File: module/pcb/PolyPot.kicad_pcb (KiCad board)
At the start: 2 copper layers, 50 x 50 mm, 34 parts, among them J1 V_BAT_1S, J2 PROG/DEBUG, J3 ANALOG_CONN, J4 TOF_DIST_SENS, J5 M3, J6 M3, J7 M3, J8 M3, M1 DC_WATER_PUMP, Q1 Q_NMOS_DGS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

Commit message: Update pin assignment, add user button, add luminosity conn
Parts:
- added J9: LUMINOSITY_CONN, Socket_Strips:Socket_Strip_Straight_1x03_Pitch2.00mm, F.Cu at (63.5, 103.0)
- added R7, R9: 10k, Resistors_SMD:R_0603_HandSoldering, F.Cu at (55.0, 90.1)
- added R8: 470, Resistors_SMD:R_0603_HandSoldering, F.Cu at (55.0, 90.1)
- added SW3: USR_BTN, Socket_Strips:Socket_Strip_Straight_1x02_Pitch2.00mm, F.Cu at (72.3, 92.0)
- added TP5: TEST, Socket_Strips:Socket_Strip_Straight_1x01_Pitch1.27mm, F.Cu at (55.0, 90.1)
- J3: value ANALOG_CONN -> HUMIDITY_CONN
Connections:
- D1 pad 2: (no net) -> /LED_STATUS
- J1 pad 1: (no net) -> /V_BAT_SENSE
- J3 pad 2: (no net) -> /SENS_HUMIDITY
- Q1 pad 2: (no net) -> /PUMP_PWM
- R3 pad 1: +3V3 -> (no net)
- U2 pad 1: (no net) -> GND
- U2 pad 12: (no net) -> /PUMP_PWM
- U2 pad 13: (no net) -> /LED_STATUS
- U2 pad 14: (no net) -> /SENSORS_ENn
- U2 pad 24: (no net) -> Net-(R7-Pad2)
- U2 pad 30: (no net) -> /I2C_SDA
- U2 pad 31: (no net) -> /I2C_SCL
- U2 pad 35: /UART_TX -> Net-(R8-Pad1)
- U2 pad 39: (no net) -> GND
- U2 pad 7: (no net) -> /V_BAT_SENSE
- U2 pad 8: (no net) -> /SENS_HUMIDITY
- U2 pad 9: (no net) -> /SENS_LUMINOSITY

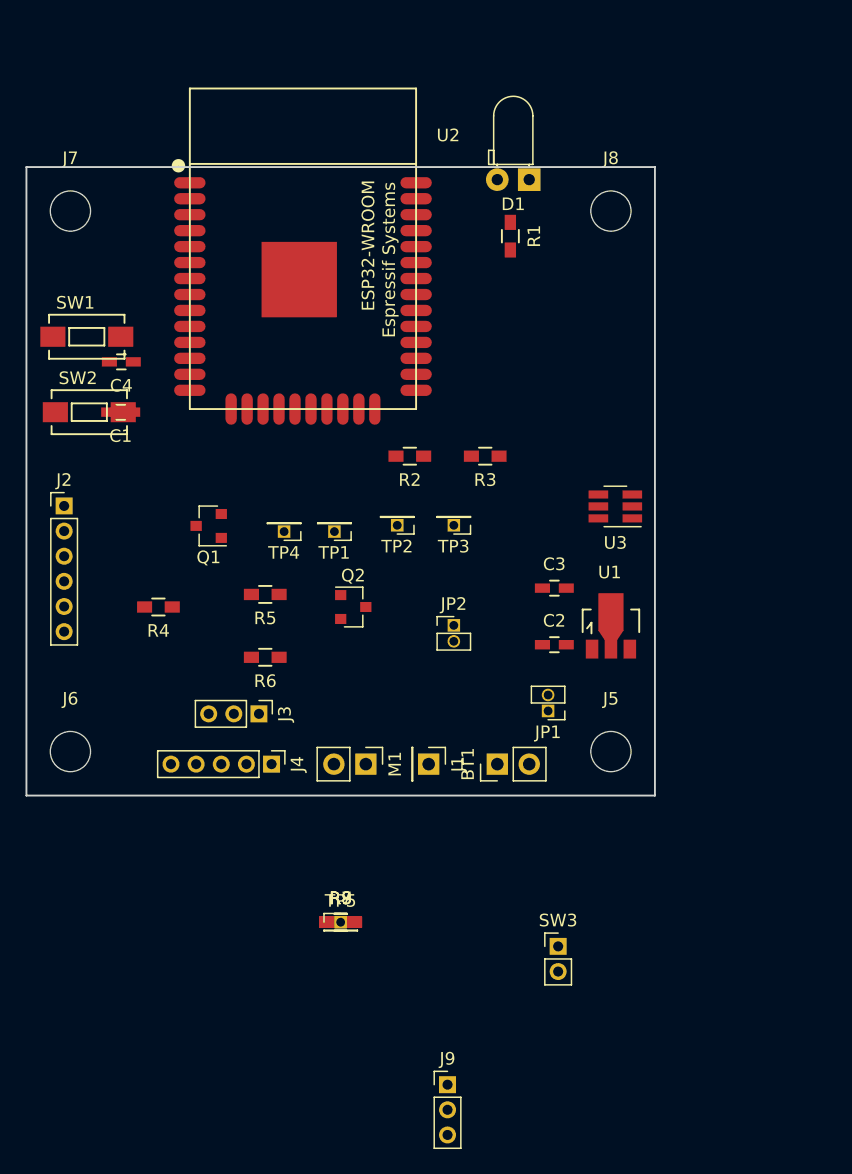
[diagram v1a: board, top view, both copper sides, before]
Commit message: PCB: update voltage regulator
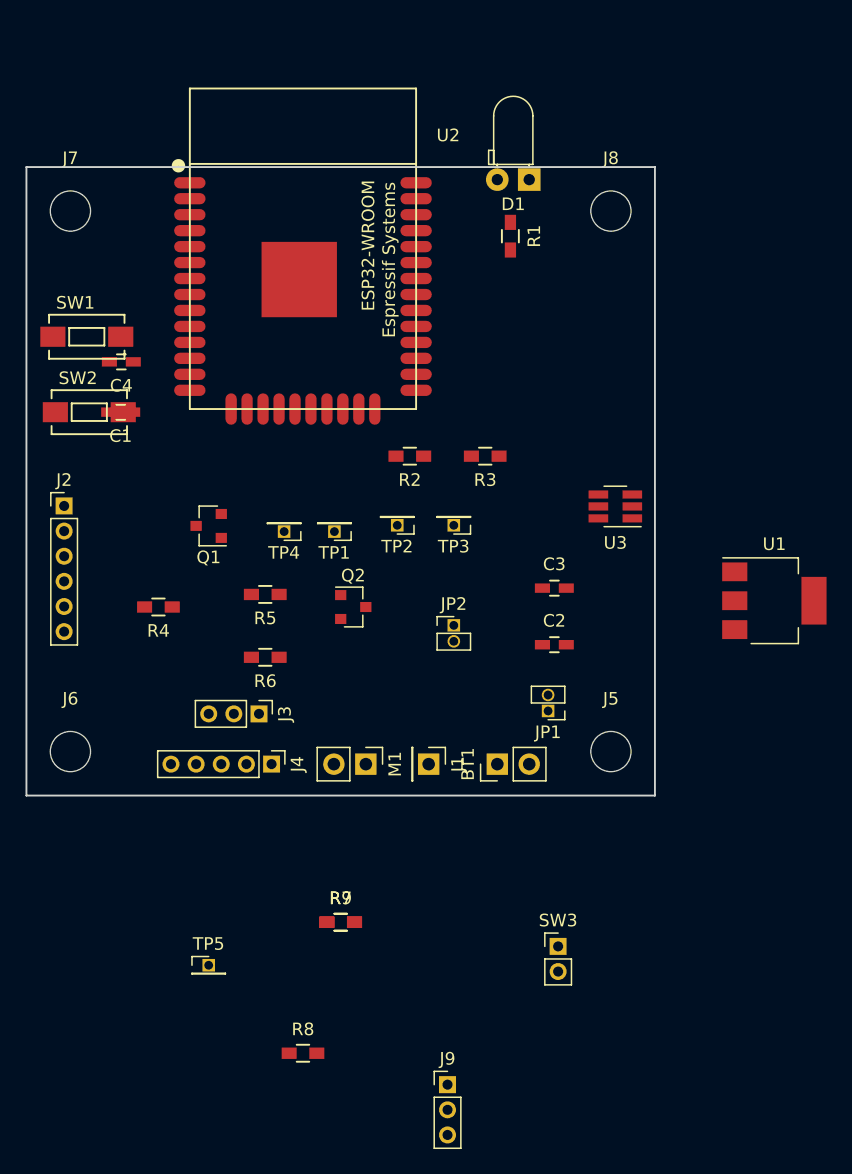
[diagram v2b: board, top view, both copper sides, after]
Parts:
- U1: value MCP1703A-3002_SOT89 -> AP7365-XXEG_SOT223; footprint TO_SOT_Packages_SMD:SOT89-3_Housing -> TO_SOT_Packages_SMD:SOT-223
- moved U1 13.2 mm to (89.5, 64.5)
- moved TP5 11.0 mm to (44.5, 93.5)
- moved R8 10.8 mm to (52.0, 100.5)
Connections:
- U1 pad 1: GND -> +3V3
- U1 pad 2: Net-(C2-Pad1) -> GND
- U1 pad 3: +3V3 -> Net-(C2-Pad1)
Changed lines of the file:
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@@
 (kicad_pcb (version 4) (host pcbnew 4.0.7)
   (general
-    (links 72)
-    (no_connects 72)
+    (links 70)
+    (no_connects 70)
     (area 29.924999 29.924999 80.075001 80.075001)
     (thickness 1.6)
@@
     (pad 1 smd rect (at -2.7 0) (size 2 1.6) (layers F.Cu F.Paste F.Mask)
       (net 2 GND))
-  )
-  (module TO_SOT_Packages_SMD:SOT89-3_Housing (layer F.Cu)
-    (at 76.5 66.5)
-    (descr "SOT89-3, Housing,")
-    (tags "SOT89-3, Housing,")
-    (attr smd)
-    (fp_text reference U1 (at -0.09906 -4.24942) (layer F.SilkS)
-      (effects (font (size 1 1) (thickness 0.15)))
-    )
-    (fp_text value MCP1703A-3002_SOT89 (at -0.20066 4.59994) (layer F.Fab)
-      (effects (font (size 1 1) (thickness 0.15)))
-    )
-    (fp_line (start -1.89992 0.20066) (end -1.651 -0.09906) (layer F.SilkS) (width 0.15))
-    (fp_line (start -1.651 -0.09906) (end -1.5494 -0.24892) (layer F.SilkS) (width 0.15))
-    (fp_line (start -1.5494 -0.24892) (end -1.5494 0.59944) (layer F.SilkS) (width 0.15))
-    (fp_line (start -2.25044 -1.30048) (end -2.25044 0.50038) (layer F.SilkS) (width 0.15))
-    (fp_line (start -2.25044 -1.30048) (end -1.6002 -1.30048) (layer F.SilkS) (width 0.15))
-    (fp_line (start 2.25044 -1.30048) (end 2.25044 0.50038) (layer F.SilkS) (width 0.15))
-    (fp_line (start 2.25044 -1.30048) (end 1.6002 -1.30048) (layer F.SilkS) (width 0.15))
-    (pad 1 smd rect (at -1.50114 1.85166) (size 1.00076 1.50114) (layers F.Cu F.Paste F.Mask)
-      (net 2 GND))
-    (pad 2 smd rect (at 0 1.85166) (size 1.00076 1.50114) (layers F.Cu F.Paste F.Mask)
-      (net 4 "Net-(C2-Pad1)"))
-    (pad 3 smd rect (at 1.50114 1.85166) (size 1.00076 1.50114) (layers F.Cu F.Paste F.Mask)
-      (net 3 +3V3))
-    (pad 2 smd rect (at 0 -1.09982) (size 1.99898 2.99974) (layers F.Cu F.Paste F.Mask)
-      (net 4 "Net-(C2-Pad1)"))
-    (pad 2 smd trapezoid (at 0 0.7493 180) (size 1.50114 0.7493) (rect_delta 0 0.50038 ) (layers F.Cu F.Paste F.Mask)
-      (net 4 "Net-(C2-Pad1)"))
-    (model TO_SOT_Packages_SMD.3dshapes/SOT89-3_Housing.wrl
-      (at (xyz 0 0 0))
-      (scale (xyz 0.3937 0.3937 0.3937))
-      (rotate (xyz 0 0 0))
-    )
   )
   (module PolyPot:ESP32-WROOM (layer F.Cu)
@@
   )
   (module Resistors_SMD:R_0603_HandSoldering (layer F.Cu)
-    (at 55 90.075001)
+    (at 52 100.5)
     (descr "Resistor SMD 0603, hand soldering")
     (tags "resistor 0603")
@@
   )
   (module Socket_Strips:Socket_Strip_Straight_1x01_Pitch1.27mm (layer F.Cu)
-    (at 55 90.075001)
+    (at 44.5 93.5)
     (descr "Through hole straight socket strip, 1x01, 1.27mm pitch, single row")
     (tags "Through hole socket strip THT 1x01 1.27mm single row")
@@
     )
   )
+  (module TO_SOT_Packages_SMD:SOT-223 (layer F.Cu)
+    (at 89.5 64.5)
+    (descr "module CMS SOT223 4 pins")
+    (tags "CMS SOT")
+    (attr smd)
+    (fp_text reference U1 (at 0 -4.5) (layer F.SilkS)
+      (effects (font (size 1 1) (thickness 0.15)))
+    )
+    (fp_text value AP7365-XXEG_SOT223 (at 0 4.5) (layer F.Fab)
+      (effects (font (size 1 1) (thickness 0.15)))
+    )
+    (fp_line (start 1.91 3.41) (end 1.91 2.15) (layer F.SilkS) (width 0.12))
+    (fp_line (start 1.91 -3.41) (end 1.91 -2.15) (layer F.SilkS) (width 0.12))
+    (fp_line (start 4.4 -3.6) (end -4.4 -3.6) (layer F.CrtYd) (width 0.05))
+    (fp_line (start 4.4 3.6) (end 4.4 -3.6) (layer F.CrtYd) (width 0.05))
+    (fp_line (start -4.4 3.6) (end 4.4 3.6) (layer F.CrtYd) (width 0.05))
+    (fp_line (start -4.4 -3.6) (end -4.4 3.6) (layer F.CrtYd) (width 0.05))
+    (fp_line (start -1.85 -3.35) (end -1.85 3.35) (layer F.Fab) (width 0.15))
+    (fp_line (start -1.85 3.41) (end 1.91 3.41) (layer F.SilkS) (width 0.12))
+    (fp_line (start -1.85 -3.35) (end 1.85 -3.35) (layer F.Fab) (width 0.15))
+    (fp_line (start -4.1 -3.41) (end 1.91 -3.41) (layer F.SilkS) (width 0.12))
+    (fp_line (start -1.85 3.35) (end 1.85 3.35) (layer F.Fab) (width 0.15))
+    (fp_line (start 1.85 -3.35) (end 1.85 3.35) (layer F.Fab) (width 0.15))
+    (pad 4 smd rect (at 3.15 0) (size 2 3.8) (layers F.Cu F.Paste F.Mask))
+    (pad 2 smd rect (at -3.15 0) (size 2 1.5) (layers F.Cu F.Paste F.Mask)
+      (net 2 GND))
+    (pad 3 smd rect (at -3.15 2.3) (size 2 1.5) (layers F.Cu F.Paste F.Mask)
+      (net 4 "Net-(C2-Pad1)"))
+    (pad 1 smd rect (at -3.15 -2.3) (size 2 1.5) (layers F.Cu F.Paste F.Mask)
+      (net 3 +3V3))
+    (model TO_SOT_Packages_SMD.3dshapes/SOT-223.wrl
+      (at (xyz 0 0 0))
+      (scale (xyz 0.4 0.4 0.4))
+      (rotate (xyz 0 0 90))
+    )
+  )

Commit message: PCB: 3d model placement
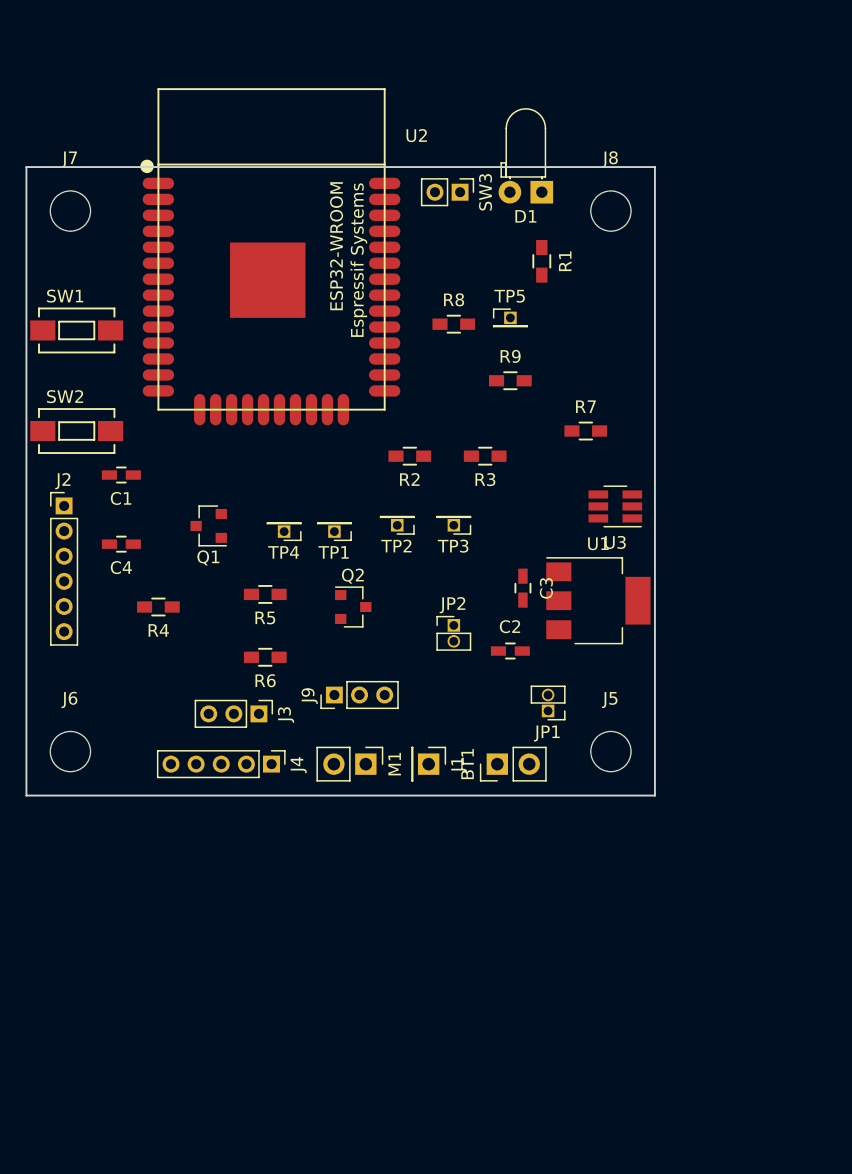
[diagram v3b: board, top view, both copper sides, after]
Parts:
- moved SW3 60.5 mm to (64.5, 32.0), turned to 270 degrees
- moved R8 59.2 mm to (64.0, 42.5)
- moved TP5 56.8 mm to (68.5, 42.0)
- moved R9 45.1 mm to (68.5, 47.0)
- moved R7 43.7 mm to (74.5, 51.0)
- moved J9 32.3 mm to (54.5, 72.0), turned to 90 degrees
- moved C4 14.5 mm to (37.5, 60.0)
- moved U1 14.0 mm to (75.5, 64.5)
- moved C1 5.00 mm to (37.5, 54.5)
- moved C2 3.54 mm to (68.5, 68.5)
- moved R1 3.20 mm to (71.0, 37.5)
- moved U2 2.50 mm to (49.5, 36.5)
- moved C3 2.50 mm to (69.5, 63.5), turned to 270 degrees
- moved SW2 1.80 mm to (34.0, 51.0)
- moved D1 1.41 mm to (71.0, 32.0)
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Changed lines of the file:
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@@
   )
   (module Capacitors_SMD:C_0603_HandSoldering (layer F.Cu)
-    (at 37.5 49.5 180)
+    (at 37.55 54.5 180)
     (descr "Capacitor SMD 0603, hand soldering")
     (tags "capacitor 0603")
@@
   )
   (module Capacitors_SMD:C_0603_HandSoldering (layer F.Cu)
-    (at 72 68)
+    (at 68.5 68.5)
     (descr "Capacitor SMD 0603, hand soldering")
     (tags "capacitor 0603")
@@
   )
   (module Capacitors_SMD:C_0603_HandSoldering (layer F.Cu)
-    (at 72 63.5)
+    (at 69.5 63.5 270)
     (descr "Capacitor SMD 0603, hand soldering")
     (tags "capacitor 0603")
     (attr smd)
-    (fp_text reference C3 (at 0 -1.9) (layer F.SilkS)
-      (effects (font (size 1 1) (thickness 0.15)))
-    )
-    (fp_text value 1uF (at 0 1.9) (layer F.Fab)
+    (fp_text reference C3 (at 0 -1.9 270) (layer F.SilkS)
+      (effects (font (size 1 1) (thickness 0.15)))
+    )
+    (fp_text value 1uF (at 0 1.9 270) (layer F.Fab)
       (effects (font (size 1 1) (thickness 0.15)))
     )
@@
     (fp_line (start -0.35 -0.6) (end 0.35 -0.6) (layer F.SilkS) (width 0.15))
     (fp_line (start 0.35 0.6) (end -0.35 0.6) (layer F.SilkS) (width 0.15))
-    (pad 1 smd rect (at -0.95 0) (size 1.2 0.75) (layers F.Cu F.Paste F.Mask)
+    (pad 1 smd rect (at -0.95 0 270) (size 1.2 0.75) (layers F.Cu F.Paste F.Mask)
       (net 3 +3V3))
-    (pad 2 smd rect (at 0.95 0) (size 1.2 0.75) (layers F.Cu F.Paste F.Mask)
+    (pad 2 smd rect (at 0.95 0 270) (size 1.2 0.75) (layers F.Cu F.Paste F.Mask)
       (net 2 GND))
     (model Capacitors_SMD.3dshapes/C_0603_HandSoldering.wrl
@@
   )
   (module Capacitors_SMD:C_0603_HandSoldering (layer F.Cu)
-    (at 37.55 45.5 180)
+    (at 37.55 60 180)
     (descr "Capacitor SMD 0603, hand soldering")
     (tags "capacitor 0603")
@@
       (at (xyz 0 0 0))
       (scale (xyz 1 1 1))
-      (rotate (xyz 0 0 90))
+      (rotate (xyz 0 0 0))
     )
   )
@@
       (at (xyz 0 0 0))
       (scale (xyz 1 1 1))
-      (rotate (xyz 0 0 90))
+      (rotate (xyz 0 0 0))
     )
   )
   (module Resistors_SMD:R_0603_HandSoldering (layer F.Cu)
-    (at 68.5 35.5 270)
+    (at 71 37.5 270)
     (descr "Resistor SMD 0603, hand soldering")
     (tags "resistor 0603")
@@
   )
   (module Buttons_Switches_SMD:SW_SPST_EVQPE1 (layer F.Cu)
-    (at 34.8 43.5)
+    (at 34 43)
     (descr "Light Touch Switch")
     (attr smd)
@@
   )
   (module Buttons_Switches_SMD:SW_SPST_EVQPE1 (layer F.Cu)
-    (at 35 49.5)
+    (at 34 51)
     (descr "Light Touch Switch")
     (attr smd)
@@
   )
   (module PolyPot:ESP32-WROOM (layer F.Cu)
-    (at 52 36.5 180)
+    (at 49.5 36.55 180)
     (fp_text reference U2 (at -11.557 9.017 180) (layer F.SilkS)
       (effects (font (size 1 1) (thickness 0.15)))
@@
   )
   (module LEDs:LED_D3.0mm_Horizontal_O1.27mm_Z2.0mm (layer F.Cu)
-    (at 70 31 180)
+    (at 71 32 180)
     (descr "LED, diameter 3.0mm z-position of LED center 2.0mm, 2 pins")
     (tags "LED diameter 3.0mm z-position of LED center 2.0mm 2 pins")
@@
   )
   (module Socket_Strips:Socket_Strip_Straight_1x03_Pitch2.00mm (layer F.Cu)
-    (at 63.5 103)
+    (at 54.5 72 90)
     (descr "Through hole straight socket strip, 1x03, 2.00mm pitch, single row")
     (tags "Through hole socket strip THT 1x03 2.00mm single row")
-    (fp_text reference J9 (at 0 -2.06) (layer F.SilkS)
-      (effects (font (size 1 1) (thickness 0.15)))
-    )
-    (fp_text value LUMINOSITY_CONN (at 0 6.06) (layer F.Fab)
+    (fp_text reference J9 (at 0 -2.06 90) (layer F.SilkS)
+      (effects (font (size 1 1) (thickness 0.15)))
+    )
+    (fp_text value LUMINOSITY_CONN (at 0 6.06 90) (layer F.Fab)
       (effects (font (size 1 1) (thickness 0.15)))
     )
@@
     (fp_line (start 1.5 5.5) (end 1.5 -1.5) (layer F.CrtYd) (width 0.05))
     (fp_line (start 1.5 -1.5) (end -1.5 -1.5) (layer F.CrtYd) (width 0.05))
-    (fp_text user %R (at 0 -2.06) (layer F.Fab)
-      (effects (font (size 1 1) (thickness 0.15)))
-    )
-    (pad 1 thru_hole rect (at 0 0) (size 1.35 1.35) (drill 0.8) (layers *.Cu *.Mask)
+    (fp_text user %R (at 0 -2.06 90) (layer F.Fab)
+      (effects (font (size 1 1) (thickness 0.15)))
+    )
+    (pad 1 thru_hole rect (at 0 0 90) (size 1.35 1.35) (drill 0.8) (layers *.Cu *.Mask)
       (net 5 /3V3_SENSORS))
-    (pad 2 thru_hole oval (at 0 2) (size 1.35 1.35) (drill 0.8) (layers *.Cu *.Mask)
+    (pad 2 thru_hole oval (at 0 2 90) (size 1.35 1.35) (drill 0.8) (layers *.Cu *.Mask)
       (net 19 /SENS_LUMINOSITY))
-    (pad 3 thru_hole oval (at 0 4) (size 1.35 1.35) (drill 0.8) (layers *.Cu *.Mask)
+    (pad 3 thru_hole oval (at 0 4 90) (size 1.35 1.35) (drill 0.8) (layers *.Cu *.Mask)
       (net 2 GND))
     (model ${KISYS3DMOD}/Socket_Strips.3dshapes/Socket_Strip_Straight_1x03_Pitch2.00mm.wrl
@@
   )
   (module Resistors_SMD:R_0603_HandSoldering (layer F.Cu)
-    (at 55 90.075001)
+    (at 74.5 51)
     (descr "Resistor SMD 0603, hand soldering")
     (tags "resistor 0603")
@@
   )
   (module Resistors_SMD:R_0603_HandSoldering (layer F.Cu)
-    (at 52 100.5)
+    (at 64 42.5)
     (descr "Resistor SMD 0603, hand soldering")
     (tags "resistor 0603")
@@
   )
   (module Resistors_SMD:R_0603_HandSoldering (layer F.Cu)
-    (at 55 90.075001)
+    (at 68.5 47)
     (descr "Resistor SMD 0603, hand soldering")
     (tags "resistor 0603")
@@
   )
   (module Socket_Strips:Socket_Strip_Straight_1x01_Pitch1.27mm (layer F.Cu)
-    (at 44.5 93.5)
+    (at 68.5 42)
     (descr "Through hole straight socket strip, 1x01, 1.27mm pitch, single row")
     (tags "Through hole socket strip THT 1x01 1.27mm single row")
@@
   )
   (module Socket_Strips:Socket_Strip_Straight_1x02_Pitch2.00mm (layer F.Cu)
-    (at 72.3 92)
+    (at 64.5 32 270)
     (descr "Through hole straight socket strip, 1x02, 2.00mm pitch, single row")
     (tags "Through hole socket strip THT 1x02 2.00mm single row")
-    (fp_text reference SW3 (at 0 -2.06) (layer F.SilkS)
-      (effects (font (size 1 1) (thickness 0.15)))
-    )
-    (fp_text value USR_BTN (at 0 4.06) (layer F.Fab)
+    (fp_text reference SW3 (at 0 -2.06 270) (layer F.SilkS)
+      (effects (font (size 1 1) (thickness 0.15)))
+    )
+    (fp_text value USR_BTN (at 0 4.06 270) (layer F.Fab)
       (effects (font (size 1 1) (thickness 0.15)))
     )
@@
     (fp_line (start 1.5 3.5) (end 1.5 -1.5) (layer F.CrtYd) (width 0.05))
     (fp_line (start 1.5 -1.5) (end -1.5 -1.5) (layer F.CrtYd) (width 0.05))
-    (fp_text user %R (at 0 -2.06) (layer F.Fab)
-      (effects (font (size 1 1) (thickness 0.15)))
-    )
-    (pad 1 thru_hole rect (at 0 0) (size 1.35 1.35) (drill 0.8) (layers *.Cu *.Mask)
-      (net 2 GND))
-    (pad 2 thru_hole oval (at 0 2) (size 1.35 1.35) (drill 0.8) (layers *.Cu *.Mask)
+    (fp_text user %R (at 0 -2.06 270) (layer F.Fab)
+      (effects (font (size 1 1) (thickness 0.15)))
+    )
+    (pad 1 thru_hole rect (at 0 0 270) (size 1.35 1.35) (drill 0.8) (layers *.Cu *.Mask)
+      (net 2 GND))
+    (pad 2 thru_hole oval (at 0 2 270) (size 1.35 1.35) (drill 0.8) (layers *.Cu *.Mask)
       (net 23 /USER_BUTTON))
     (model ${KISYS3DMOD}/Socket_Strips.3dshapes/Socket_Strip_Straight_1x02_Pitch2.00mm.wrl
@@
   )
   (module TO_SOT_Packages_SMD:SOT-223 (layer F.Cu)
-    (at 89.5 64.5)
+    (at 75.5 64.5)
     (descr "module CMS SOT223 4 pins")
     (tags "CMS SOT")
@@
     (model TO_SOT_Packages_SMD.3dshapes/SOT-223.wrl
       (at (xyz 0 0 0))
-      (scale (xyz 0.4 0.4 0.4))
-      (rotate (xyz 0 0 90))
-    )
-  )
+      (scale (xyz 1 1 1))
+      (rotate (xyz 0 0 0))
+    )
+  )
